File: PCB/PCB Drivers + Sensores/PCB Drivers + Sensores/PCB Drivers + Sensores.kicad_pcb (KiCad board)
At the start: 2 copper layers, 44 parts, among them J1 Power, J10 Conn_01x04, J11 Conn_01x04, J12 Conn_01x04, J13 Conn_01x04, J14 Screw_Terminal_01x02, J16 Screw_Terminal_01x02, J17 Conn_01x02, J2 PWM, J3 Analog, J4 PWM, J5 Analog, J6 Communication, J7 Digital, J8 Conn_01x04, J9 Conn_01x04

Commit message: Multplex + Sensores
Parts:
- added Sensor_1: Conn_01x07, Connector_PinSocket_2.54mm:PinSocket_1x07_P2.54mm_Vertical, F.Cu at (111.0, 82.6)
- added Sensor_10: Conn_01x07, Connector_PinSocket_2.54mm:PinSocket_1x07_P2.54mm_Vertical, F.Cu at (181.9, 82.6)
- added Sensor_11: Conn_01x07, Connector_PinSocket_2.54mm:PinSocket_1x07_P2.54mm_Vertical, F.Cu at (189.8, 82.6)
- added Sensor_12: Conn_01x07, Connector_PinSocket_2.54mm:PinSocket_1x07_P2.54mm_Vertical, F.Cu at (197.7, 82.6)
- added Sensor_2: Conn_01x07, Connector_PinSocket_2.54mm:PinSocket_1x07_P2.54mm_Vertical, F.Cu at (118.9, 82.6)
- added Sensor_3: Conn_01x07, Connector_PinSocket_2.54mm:PinSocket_1x07_P2.54mm_Vertical, F.Cu at (126.8, 82.6)
- added Sensor_4: Conn_01x07, Connector_PinSocket_2.54mm:PinSocket_1x07_P2.54mm_Vertical, F.Cu at (134.6, 82.6)
- added Sensor_5: Conn_01x07, Connector_PinSocket_2.54mm:PinSocket_1x07_P2.54mm_Vertical, F.Cu at (142.5, 82.6)
- added Sensor_6: Conn_01x07, Connector_PinSocket_2.54mm:PinSocket_1x07_P2.54mm_Vertical, F.Cu at (150.4, 82.6)
- added Sensor_7: Conn_01x07, Connector_PinSocket_2.54mm:PinSocket_1x07_P2.54mm_Vertical, F.Cu at (158.3, 82.6)
- added Sensor_8: Conn_01x07, Connector_PinSocket_2.54mm:PinSocket_1x07_P2.54mm_Vertical, F.Cu at (166.2, 82.6)
- added Sensor_9: Conn_01x07, Connector_PinSocket_2.54mm:PinSocket_1x07_P2.54mm_Vertical, F.Cu at (174.1, 82.6)
- added U1: BOB-09056, BOB-09056:MODULE_BOB-09056, F.Cu at (154.6, 103.4)
- J7: moved to B.Cu
- moved J16 63.5 mm to (252.9, 177.1)
- moved J14 61.4 mm to (252.5, 78.8)
- moved A1 48.6 mm to (273.5, 207.3)
- moved A2 48.6 mm to (273.5, 184.4)
- moved A3 48.6 mm to (273.5, 161.5)
- moved A4 48.6 mm to (273.5, 138.6)
- moved A5 48.6 mm to (273.5, 115.7)
- moved A6 48.6 mm to (273.5, 92.8)
- moved D5 48.6 mm to (285.3, 117.2)
- moved D6 48.6 mm to (285.6, 94.4)
- moved J10 48.6 mm to (302.4, 202.3)
- moved J11 48.6 mm to (302.4, 133.5)
- moved J12 48.6 mm to (302.4, 110.6)
- moved J13 48.6 mm to (302.4, 87.6)
- moved J8 48.6 mm to (302.4, 179.4)
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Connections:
- net /SCL/21 renamed SCL
- J2 pad 10: /*8 -> LED_6
- J2 pad 5: /*13 -> LED_1
- J2 pad 6: /*12 -> LED_2
- J2 pad 7: /*11 -> LED_3
- J2 pad 8: /*10 -> LED_4
- J2 pad 9: /*9 -> LED_5
- J6 pad 1: /TX3/14 -> LED_7
- J6 pad 2: /RX3/15 -> LED_8
- J6 pad 3: /TX2/16 -> LED_9
- J6 pad 4: /RX2/17 -> LED_10
- J6 pad 5: /TX1/18 -> LED_11
- J6 pad 6: /RX1/19 -> LED_12
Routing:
- net 12V: track 194.8 -> 0.00 mm
- net 5V: track 0.00 -> 194.1 mm
- net SCL: track 0.00 -> 113.0 mm
- net LED_6: track 0.00 -> 52.6 mm
- net LED_7: track 0.00 -> 51.8 mm
- net LED_8: track 0.00 -> 50.8 mm
- net LED_5: track 0.00 -> 46.9 mm
- net SDA_12: track 0.00 -> 45.8 mm
- net SDA_1: track 0.00 -> 43.1 mm
- net LED_9: track 0.00 -> 42.8 mm
- net LED_1: track 0.00 -> 42.4 mm
- net LED_12: track 0.00 -> 41.7 mm
- net SDA_11: track 0.00 -> 41.0 mm
- net SDA_2: track 0.00 -> 41.0 mm
- net LED_4: track 0.00 -> 40.8 mm
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
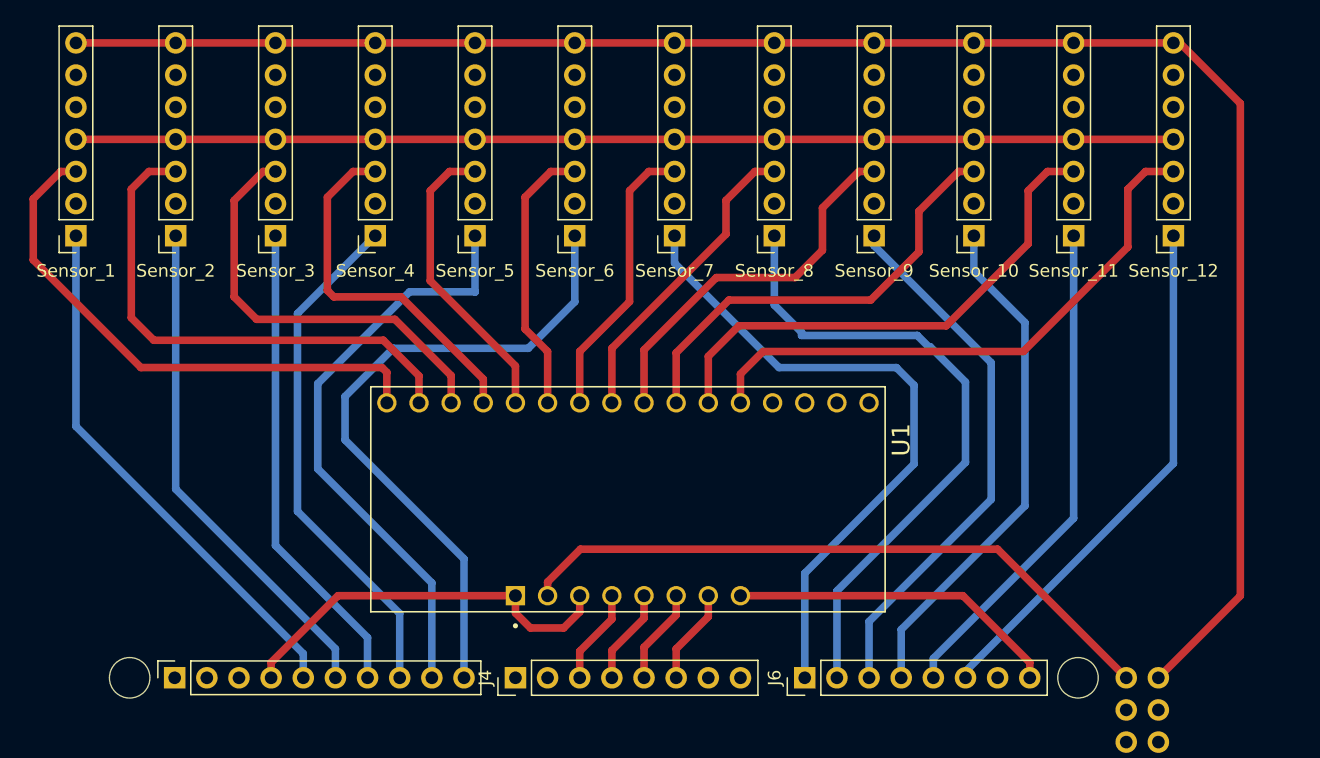
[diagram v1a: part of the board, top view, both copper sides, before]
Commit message: Versáo Teste - Trilhas Menores
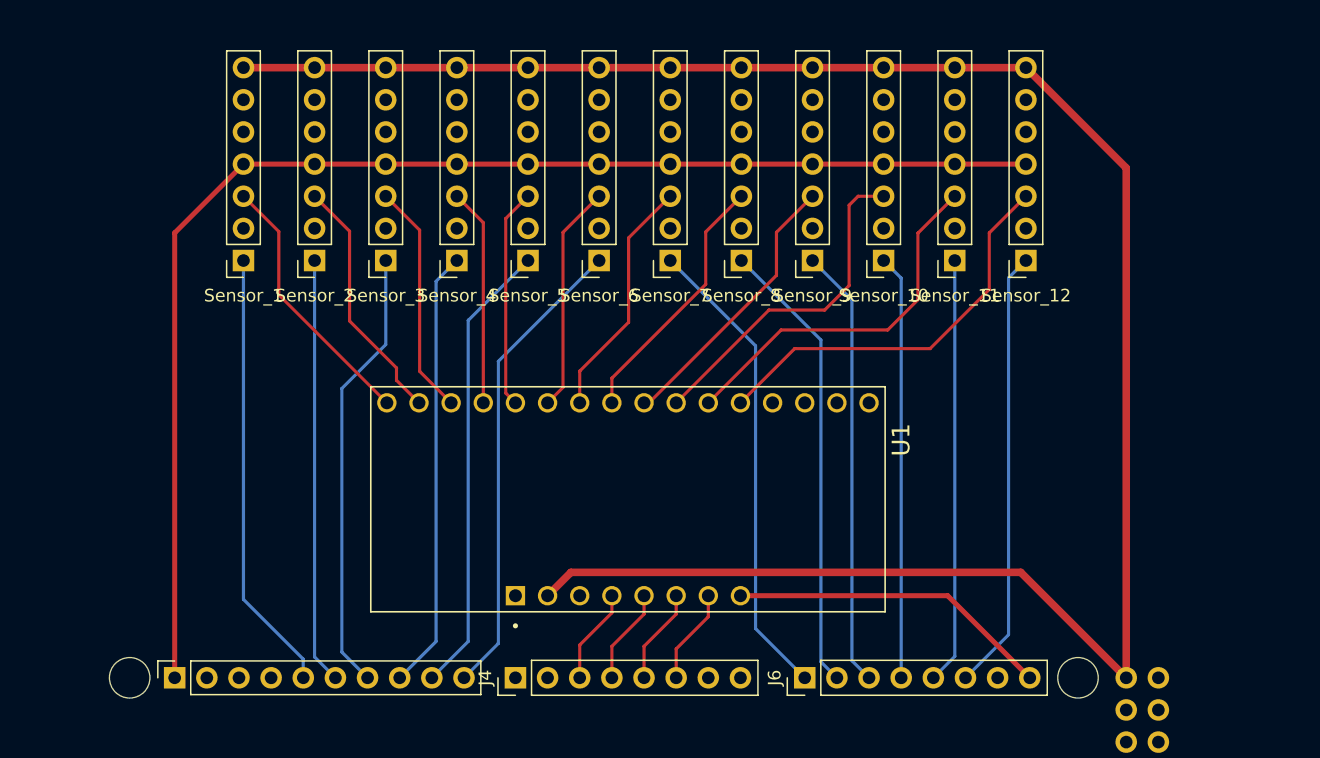
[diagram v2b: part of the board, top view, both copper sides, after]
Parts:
- moved Sensor_1 13.4 mm to (124.2, 84.6)
- moved Sensor_12 11.8 mm to (186.1, 84.6)
- moved Sensor_2 11.1 mm to (129.9, 84.6)
- moved Sensor_11 9.59 mm to (180.4, 84.6)
- moved Sensor_3 8.93 mm to (135.5, 84.6)
- moved Sensor_10 7.39 mm to (174.8, 84.6)
- moved Sensor_4 6.74 mm to (141.1, 84.6)
- moved Sensor_9 5.24 mm to (169.2, 84.6)
- moved Sensor_5 4.62 mm to (146.7, 84.6)
- moved Sensor_8 3.26 mm to (163.6, 84.6)
- moved Sensor_6 2.74 mm to (152.3, 84.6)
- moved Sensor_7 1.99 mm to (158.0, 84.6)
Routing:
- net GND: track 31.4 -> 0.00 mm
- net 5V: track 194.1 -> 163.3 mm
- net SDA_1: track 43.1 -> 21.0 mm
- net SDA_2: track 41.0 -> 19.7 mm
- net SCL: track 113.0 -> 130.2 mm
- net SDA_3: track 33.7 -> 18.5 mm
- net LED_6: track 52.6 -> 37.4 mm
- net LED_8: track 50.8 -> 36.1 mm
- net LED_7: track 51.8 -> 37.4 mm
- net SDA_12: track 45.8 -> 31.9 mm
- net SDA_4: track 29.1 -> 17.2 mm
- net SDA_11: track 41.0 -> 29.3 mm
- net LED_5: track 46.9 -> 36.1 mm
- net SDA_10: track 35.3 -> 26.9 mm
- net SDA_9: track 30.2 -> 22.1 mm
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
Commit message: Versão Final - V1
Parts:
- removed J10, J11, J12, J13, J8, J9: Conn_01x04, Connector_PinSocket_2.54mm:PinSocket_1x04_P2.54mm_Vertical
- removed J14, J16: Screw_Terminal_01x02, TerminalBlock_RND:TerminalBlock_RND_205-00298_1x02_P10.00mm_Horizontal
- removed J17: Conn_01x02, Connector_PinSocket_2.54mm:PinSocket_1x02_P2.54mm_Vertical
- added C1: 100uF, Capacitor_THT:CP_Radial_D8.0mm_P3.50mm, F.Cu at (134.0, 190.4)
- added C2: 100uF, Capacitor_THT:CP_Radial_D8.0mm_P3.50mm, F.Cu at (164.1, 190.4)
- added C3: 100uF, Capacitor_THT:CP_Radial_D8.0mm_P3.50mm, F.Cu at (194.3, 190.4)
- added C4: 100uF, Capacitor_THT:CP_Radial_D8.0mm_P3.50mm, F.Cu at (222.8, 159.1)
- added C5: 100uF, Capacitor_THT:CP_Radial_D8.0mm_P3.50mm, F.Cu at (222.7, 129.2)
- added C6: 100uF, Capacitor_THT:CP_Radial_D8.0mm_P3.50mm, F.Cu at (222.7, 99.2)
- added Conn_+12V_1: Screw_Terminal_01x02, TerminalBlock_RND:TerminalBlock_RND_205-00298_1x02_P10.00mm_Horizontal, F.Cu at (215.1, 205.5)
- added Driver_Conn_1: Conn_01x04, Connector_JST:JST_XH_B4B-XH-A_1x04_P2.50mm_Vertical, F.Cu at (117.1, 199.8)
- added Driver_Conn_2: Conn_01x04, Connector_JST:JST_XH_B4B-XH-A_1x04_P2.50mm_Vertical, F.Cu at (147.0, 199.8)
- added Driver_Conn_3: Conn_01x04, Connector_JST:JST_XH_B4B-XH-A_1x04_P2.50mm_Vertical, F.Cu at (177.1, 199.8)
- added Driver_Conn_4: Conn_01x04, Connector_JST:JST_XH_B4B-XH-A_1x04_P2.50mm_Vertical, F.Cu at (232.3, 176.1)
- added Driver_Conn_5: Conn_01x04, Connector_JST:JST_XH_B4B-XH-A_1x04_P2.50mm_Vertical, F.Cu at (232.3, 146.2)
- added Driver_Conn_6: Conn_01x04, Connector_JST:JST_XH_B4B-XH-A_1x04_P2.50mm_Vertical, F.Cu at (232.4, 116.2)
- added G***: LOGO, Footprints de Logos:UNICAMO_Logo, F.Cu at (232.5, 82.2)
- added JConn_+12V_2: Screw_Terminal_01x02, TerminalBlock_RND:TerminalBlock_RND_205-00298_1x02_P10.00mm_Horizontal, F.Cu at (232.3, 205.5)
- H1, H2, H3, H4: footprint MountingHole:MountingHole_2mm -> MountingHole:MountingHole_6mm
- J1, J3, J4, J5, J6: footprint Connector_PinHeader_2.54mm:PinHeader_1x08_P2.54mm_Vertical -> Connector_PinSocket_2.54mm:PinSocket_1x08_P2.54mm_Vertical
- J7: footprint Connector_PinHeader_2.54mm:PinHeader_2x18_P2.54mm_Vertical -> Connector_PinSocket_2.54mm:PinSocket_2x18_P2.54mm_Vertical; moved to F.Cu
- Sensor_1, Sensor_10, Sensor_11, Sensor_12, Sensor_2, Sensor_3, Sensor_4, Sensor_5, Sensor_6, Sensor_7, Sensor_8, Sensor_9: value Conn_01x07 -> Conn_01x05; footprint Connector_PinSocket_2.54mm:PinSocket_1x07_P2.54mm_Vertical -> Connector_JST:JST_XH_B5B-XH-A_1x05_P2.50mm_Vertical
- moved H1 192.3 mm to (243.7, 66.4)
- moved A1 162.4 mm to (112.0, 190.3), turned to 90 degrees
- moved R1 152.5 mm to (137.1, 208.2), turned to 180 degrees
- moved D1 152.0 mm to (133.3, 199.8)
- moved H2 150.0 mm to (106.3, 66.3)
- moved A2 131.8 mm to (141.9, 190.4), turned to 90 degrees
- moved H3 127.9 mm to (243.6, 208.6)
- moved R2 124.3 mm to (167.3, 208.2), turned to 180 degrees
- moved D2 122.3 mm to (163.5, 199.8)
- moved A3 105.6 mm to (172.0, 190.4), turned to 90 degrees
- moved R3 103.2 mm to (197.1, 208.2), turned to 180 degrees
- moved D3 98.9 mm to (193.3, 199.8)
- moved A4 66.2 mm to (222.8, 181.2)
- moved A5 62.0 mm to (222.7, 151.3)
- moved A6 58.1 mm to (222.8, 121.2)
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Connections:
- A1 pad 12: Net-(A1-MS3) -> unconnected-(A1-MS3-Pad12)
- A1 pad 13: unconnected-(A1-~{RESET}-Pad13) -> Net-(A1-~{RESET})
- A1 pad 14: unconnected-(A1-~{SLEEP}-Pad14) -> Net-(A1-~{RESET})
- A1 pad 15: unconnected-(A1-STEP-Pad15) -> /A1
- A1 pad 16: unconnected-(A1-DIR-Pad16) -> /A0
- A1 pad 9: unconnected-(A1-~{ENABLE}-Pad9) -> /A2
- A2 pad 12: Net-(A2-MS3) -> unconnected-(A2-MS3-Pad12)
- A2 pad 13: unconnected-(A2-~{RESET}-Pad13) -> Net-(A2-~{RESET})
- A2 pad 14: unconnected-(A2-~{SLEEP}-Pad14) -> Net-(A2-~{RESET})
- A2 pad 15: unconnected-(A2-STEP-Pad15) -> /A4
- A2 pad 16: unconnected-(A2-DIR-Pad16) -> /A3
- A2 pad 9: unconnected-(A2-~{ENABLE}-Pad9) -> /A5
- A3 pad 12: Net-(A3-MS3) -> unconnected-(A3-MS3-Pad12)
- A3 pad 13: unconnected-(A3-~{RESET}-Pad13) -> Net-(A3-~{RESET})
- A3 pad 14: unconnected-(A3-~{SLEEP}-Pad14) -> Net-(A3-~{RESET})
- A3 pad 15: unconnected-(A3-STEP-Pad15) -> /A7
- A3 pad 16: unconnected-(A3-DIR-Pad16) -> /A6
- A3 pad 9: unconnected-(A3-~{ENABLE}-Pad9) -> /A8
- A4 pad 12: Net-(A4-MS3) -> unconnected-(A4-MS3-Pad12)
- A4 pad 13: unconnected-(A4-~{RESET}-Pad13) -> Net-(A4-~{RESET})
- A4 pad 14: unconnected-(A4-~{SLEEP}-Pad14) -> Net-(A4-~{RESET})
- A4 pad 15: unconnected-(A4-STEP-Pad15) -> /51
- A4 pad 16: unconnected-(A4-DIR-Pad16) -> /53
- A4 pad 9: unconnected-(A4-~{ENABLE}-Pad9) -> /49
- A5 pad 12: Net-(A5-MS3) -> unconnected-(A5-MS3-Pad12)
- A5 pad 13: unconnected-(A5-~{RESET}-Pad13) -> Net-(A5-~{RESET})
- A5 pad 14: unconnected-(A5-~{SLEEP}-Pad14) -> Net-(A5-~{RESET})
- A5 pad 15: unconnected-(A5-STEP-Pad15) -> /41
- A5 pad 16: unconnected-(A5-DIR-Pad16) -> /43
- A5 pad 9: unconnected-(A5-~{ENABLE}-Pad9) -> /39
- A6 pad 12: Net-(A6-MS3) -> unconnected-(A6-MS3-Pad12)
- A6 pad 13: unconnected-(A6-~{RESET}-Pad13) -> Net-(A6-~{RESET})
- A6 pad 14: unconnected-(A6-~{SLEEP}-Pad14) -> Net-(A6-~{RESET})
- A6 pad 15: unconnected-(A6-STEP-Pad15) -> /27
- A6 pad 16: unconnected-(A6-DIR-Pad16) -> /29
- A6 pad 9: unconnected-(A6-~{ENABLE}-Pad9) -> /25
- D1 pad 2: Net-(A1-MS3) -> /A1
- D2 pad 2: Net-(A2-MS3) -> /A4
- D3 pad 2: Net-(A3-MS3) -> /A7
- D4 pad 2: Net-(A4-MS3) -> /51
- D5 pad 2: Net-(A5-MS3) -> /41
- D6 pad 2: Net-(A6-MS3) -> /27
- Sensor_1 pad 1: LED_1 -> 5V
- Sensor_1 pad 2: INT_1 -> GND
- Sensor_1 pad 3: SDA_1 -> SCL
- Sensor_1 pad 4: SCL -> SDA_1
- Sensor_1 pad 5: 3V3 -> LED_1
- Sensor_10 pad 1: LED_10 -> 5V
- Sensor_10 pad 2: INT_10 -> GND
- Sensor_10 pad 3: SDA_10 -> SCL
- Sensor_10 pad 4: SCL -> SDA_10
- Sensor_10 pad 5: 3V3 -> LED_10
- Sensor_11 pad 1: LED_11 -> 5V
- Sensor_11 pad 2: INT_11 -> GND
- Sensor_11 pad 3: SDA_11 -> SCL
- Sensor_11 pad 4: SCL -> SDA_11
- Sensor_11 pad 5: 3V3 -> LED_11
- Sensor_12 pad 1: LED_12 -> 5V
- Sensor_12 pad 2: INT_12 -> GND
- Sensor_12 pad 3: SDA_12 -> SCL
- Sensor_12 pad 4: SCL -> SDA_12
- Sensor_12 pad 5: 3V3 -> LED_12
- Sensor_2 pad 1: LED_2 -> 5V
- Sensor_2 pad 2: INT_2 -> GND
- Sensor_2 pad 3: SDA_2 -> SCL
- Sensor_2 pad 4: SCL -> SDA_2
- Sensor_2 pad 5: 3V3 -> LED_2
- Sensor_3 pad 1: LED_3 -> 5V
- Sensor_3 pad 2: INT_3 -> GND
- Sensor_3 pad 3: SDA_3 -> SCL
- Sensor_3 pad 4: SCL -> SDA_3
- Sensor_3 pad 5: 3V3 -> LED_3
- Sensor_4 pad 1: LED_4 -> 5V
- Sensor_4 pad 2: INT_4 -> GND
- Sensor_4 pad 3: SDA_4 -> SCL
- Sensor_4 pad 4: SCL -> SDA_4
- Sensor_4 pad 5: 3V3 -> LED_4
- Sensor_5 pad 1: LED_5 -> 5V
- Sensor_5 pad 2: INT_5 -> GND
- Sensor_5 pad 3: SDA_5 -> SCL
- Sensor_5 pad 4: SCL -> SDA_5
- Sensor_5 pad 5: 3V3 -> LED_5
- Sensor_6 pad 1: LED_6 -> 5V
- Sensor_6 pad 2: INT_6 -> GND
- Sensor_6 pad 3: SDA_6 -> SCL
- Sensor_6 pad 4: SCL -> SDA_6
- Sensor_6 pad 5: 3V3 -> LED_6
- Sensor_7 pad 1: LED_7 -> 5V
- Sensor_7 pad 2: INT_7 -> GND
- Sensor_7 pad 3: SDA_7 -> SCL
- Sensor_7 pad 4: SCL -> SDA_7
- Sensor_7 pad 5: 3V3 -> LED_7
- Sensor_8 pad 1: LED_8 -> 5V
- Sensor_8 pad 2: INT_8 -> GND
- Sensor_8 pad 3: SDA_8 -> SCL
- Sensor_8 pad 4: SCL -> SDA_8
- Sensor_8 pad 5: 3V3 -> LED_8
- Sensor_9 pad 1: LED_9 -> 5V
- Sensor_9 pad 2: INT_9 -> GND
- Sensor_9 pad 3: SDA_9 -> SCL
- Sensor_9 pad 4: SCL -> SDA_9
- Sensor_9 pad 5: 3V3 -> LED_9
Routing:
- net 5V: track 163.3 -> 483.8 mm
- net 12V: track 0.00 -> 256.6 mm
- net /A1: track 0.00 -> 82.4 mm, vias 0 -> 2
- net /51: track 0.00 -> 67.9 mm, vias 0 -> 2
- net /A4: track 0.00 -> 64.4 mm, vias 0 -> 2
- net /41: track 0.00 -> 54.9 mm, vias 0 -> 2
- net /27: track 0.00 -> 54.5 mm, vias 0 -> 2
- net /A7: track 0.00 -> 51.7 mm
- net SCL: track 130.2 -> 181.2 mm
- net /A0: track 0.00 -> 45.4 mm
- net /A2: track 0.00 -> 31.8 mm
- net LED_6: track 37.4 -> 66.5 mm
- net /53: track 0.00 -> 28.7 mm
- net SDA_12: track 31.9 -> 58.5 mm
- net LED_5: track 36.1 -> 61.0 mm
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- added copper zone on B.Cu, net GND
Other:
- board outline added: 150 x 155 mm
- board text added: "EXTENCUBE - RAIDEN"
- board text added: "J2"
- board text removed: "ICSP"

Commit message: Placa Final - +Leds +Botão
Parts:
- added D7: LED, LED_THT:LED_D5.0mm, F.Cu at (124.4, 158.0)
- added D8: LED, LED_THT:LED_D5.0mm, F.Cu at (240.4, 191.3)
- added R7: 330, Resistor_THT:R_Axial_DIN0207_L6.3mm_D2.5mm_P10.16mm_Horizontal, F.Cu at (117.8, 166.0)
- added R8: 1k, Resistor_THT:R_Axial_DIN0207_L6.3mm_D2.5mm_P10.16mm_Horizontal, F.Cu at (230.2, 184.8)
- added SW1: SW_Push, Button_Switch_THT:SW_PUSH_6mm, F.Cu at (135.1, 160.7)
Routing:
- net 12V: track 256.6 -> 269.9 mm
- net /~{RESET}: track 0.00 -> 12.4 mm
- net Net-(D7-A): track 0.00 -> 4.96 mm
- net Net-(D8-A): track 0.00 -> 3.94 mm
- net 5V: track 483.8 -> 487.3 mm
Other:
- board text added: "colocar o outro led de +12v"
- board text added: "inverter resistores e leds"
- board text added: "trocar os conectores +12v"
